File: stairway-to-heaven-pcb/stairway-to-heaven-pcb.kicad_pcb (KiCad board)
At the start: 2 copper layers, 15 parts, among them J1 Conn_01x04_Male, J2 Conn_01x04_Male, Q1 FDN337N, Q2 FDN337N, Q3 FDN337N, Q4 FDN337N, Q5 FDN337N, Q6 FDN337N, U1 MEGA_PRO_EMBED_CH340G_{slash}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

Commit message: update bom
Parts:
- moved R1 22.9 mm to (189.2, 116.8)
- moved R4 22.5 mm to (189.2, 100.3)
- moved Q1 21.6 mm to (194.3, 116.8), turned to 0 degrees
- moved Q4 21.6 mm to (194.3, 100.3), turned to 0 degrees
- moved R6 16.8 mm to (212.1, 95.2), turned to -90 degrees
- moved R3 16.7 mm to (212.1, 113.0), turned to -90 degrees
- moved Q6 11.5 mm to (217.2, 95.2), turned to 0 degrees
- moved Q3 11.4 mm to (217.2, 113.0), turned to 0 degrees
- moved R5 8.52 mm to (200.7, 97.8), turned to -90 degrees
- moved R2 8.13 mm to (200.7, 115.6)
- moved Q5 5.24 mm to (205.7, 97.8), turned to 0 degrees
- moved Q2 5.08 mm to (205.7, 115.6), turned to 0 degrees
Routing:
- net LED1B_GND: track 0.00 -> 35.7 mm
- net LED2B_GND: track 0.00 -> 33.3 mm
- net LED1B_EN: track 52.8 -> 29.7 mm
- net LED1R_GND: track 0.00 -> 22.3 mm
- net LED2R_GND: track 0.00 -> 21.9 mm
- net LED2B_EN: track 49.5 -> 29.1 mm
- net LED2G_EN: track 40.4 -> 54.7 mm
- net LED1G_EN: track 40.8 -> 53.5 mm
- net LED1G_GND: track 0.00 -> 11.8 mm
- net LED2G_GND: track 0.00 -> 10.4 mm
- net +12V: track 0.00 -> 8.62 mm
- net LED1R_EN: track 43.2 -> 37.3 mm
- net LED2R_EN: track 42.0 -> 39.1 mm

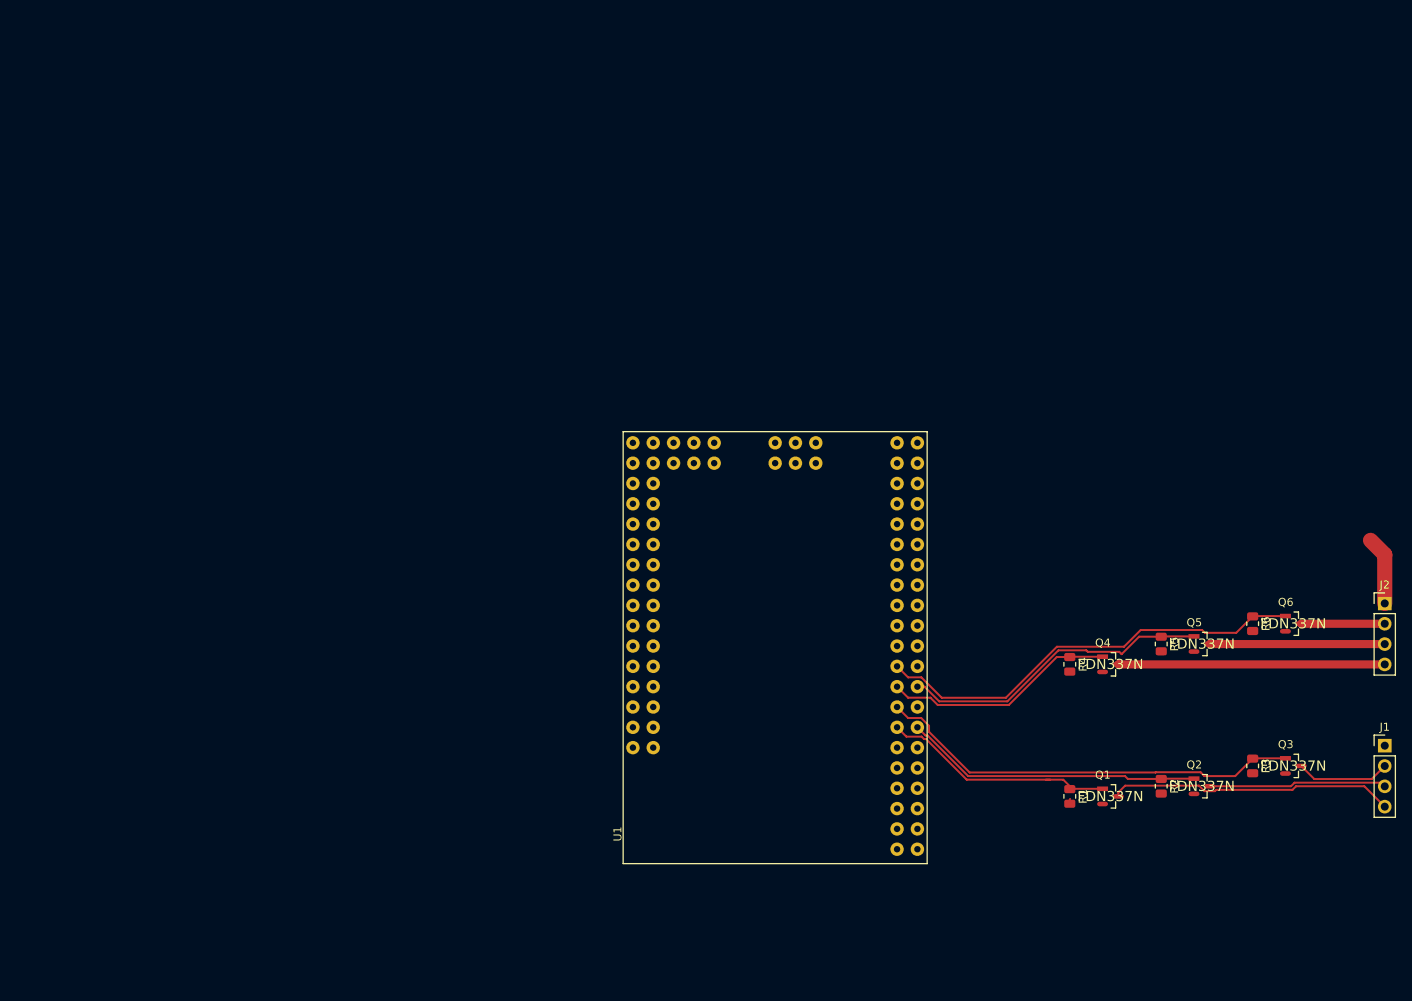
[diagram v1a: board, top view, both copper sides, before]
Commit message: Psu, hierachical pages for fet driver
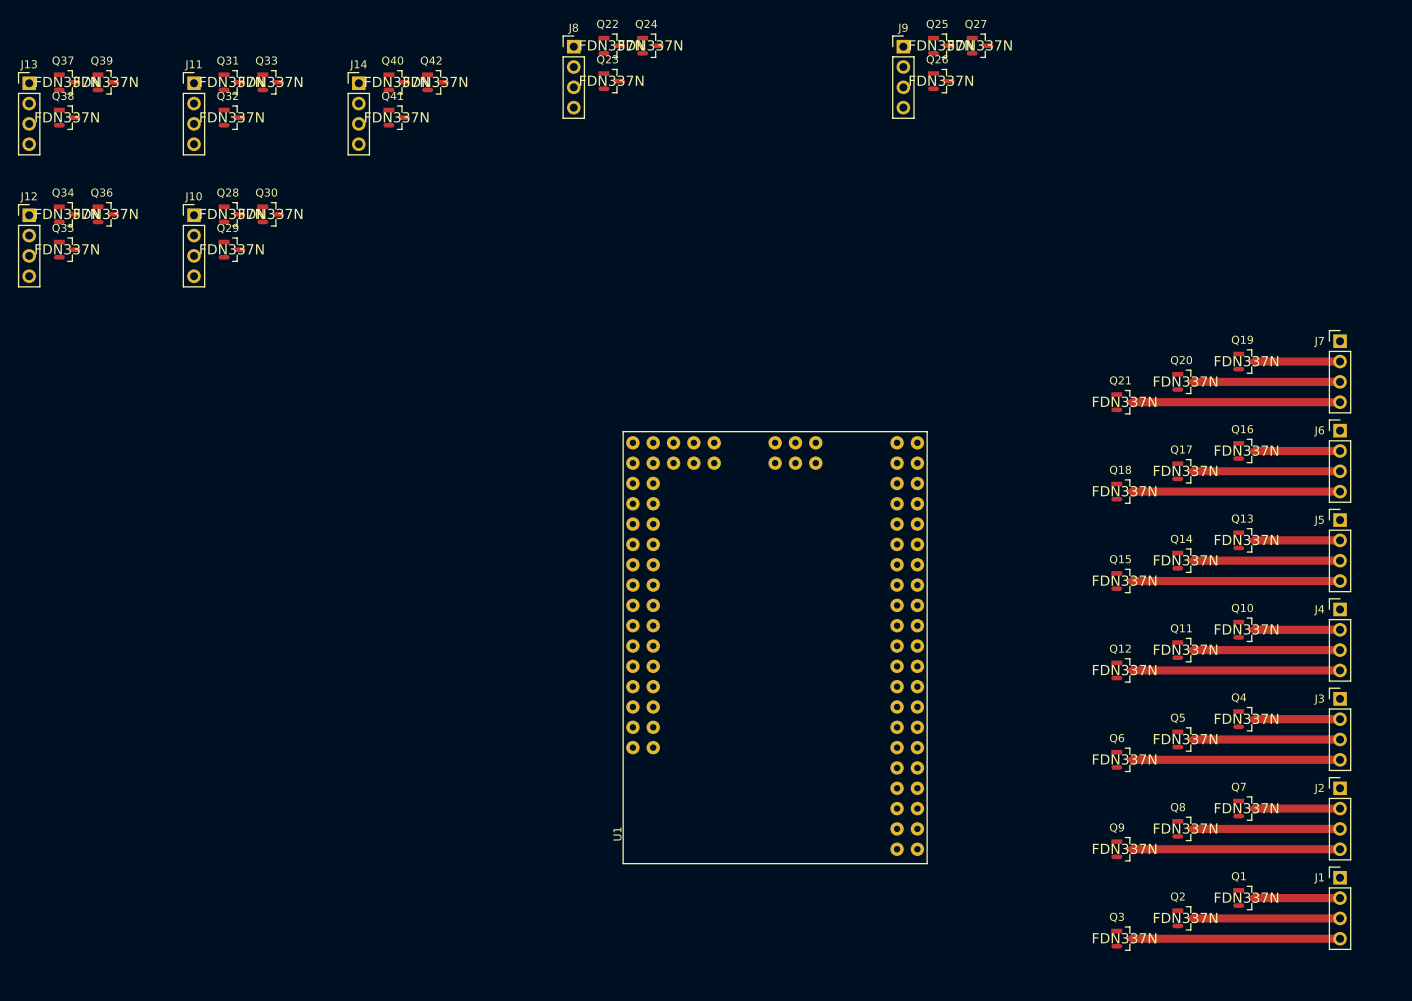
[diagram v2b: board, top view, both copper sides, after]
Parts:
- removed R1, R2, R3, R4, R5, R6: 50k, Resistor_SMD:R_0805_2012Metric
- added J10: Conn_01x04_Male, Connector_PinHeader_2.54mm:PinHeader_1x04_P2.54mm_Vertical, F.Cu at (79.8, 44.2)
- added J11: Conn_01x04_Male, Connector_PinHeader_2.54mm:PinHeader_1x04_P2.54mm_Vertical, F.Cu at (79.8, 27.7)
- added J12: Conn_01x04_Male, Connector_PinHeader_2.54mm:PinHeader_1x04_P2.54mm_Vertical, F.Cu at (59.2, 44.2)
- added J13: Conn_01x04_Male, Connector_PinHeader_2.54mm:PinHeader_1x04_P2.54mm_Vertical, F.Cu at (59.2, 27.7)
- added J14: Conn_01x04_Male, Connector_PinHeader_2.54mm:PinHeader_1x04_P2.54mm_Vertical, F.Cu at (100.4, 27.7)
- added J3: Conn_01x04_Male, Connector_PinHeader_2.54mm:PinHeader_1x04_P2.54mm_Vertical, F.Cu at (223.0, 104.6)
- added J4: Conn_01x04_Male, Connector_PinHeader_2.54mm:PinHeader_1x04_P2.54mm_Vertical, F.Cu at (223.0, 93.5)
- added J5: Conn_01x04_Male, Connector_PinHeader_2.54mm:PinHeader_1x04_P2.54mm_Vertical, F.Cu at (223.0, 82.3)
- added J6: Conn_01x04_Male, Connector_PinHeader_2.54mm:PinHeader_1x04_P2.54mm_Vertical, F.Cu at (223.0, 71.1)
- added J7: Conn_01x04_Male, Connector_PinHeader_2.54mm:PinHeader_1x04_P2.54mm_Vertical, F.Cu at (223.0, 59.9)
- added J8: Conn_01x04_Male, Connector_PinHeader_2.54mm:PinHeader_1x04_P2.54mm_Vertical, F.Cu at (127.2, 23.1)
- added J9: Conn_01x04_Male, Connector_PinHeader_2.54mm:PinHeader_1x04_P2.54mm_Vertical, F.Cu at (168.4, 23.1)
- added Q10: FDN337N, FDN337N:ON_Semi-527AG-01-12_2008-O-IPC_B, F.Cu at (211.3, 96.0)
- added Q11: FDN337N, FDN337N:ON_Semi-527AG-01-12_2008-O-IPC_B, F.Cu at (203.7, 98.6)
- added Q12: FDN337N, FDN337N:ON_Semi-527AG-01-12_2008-O-IPC_B, F.Cu at (196.1, 101.1)
- added Q13: FDN337N, FDN337N:ON_Semi-527AG-01-12_2008-O-IPC_B, F.Cu at (211.3, 84.8)
- added Q14: FDN337N, FDN337N:ON_Semi-527AG-01-12_2008-O-IPC_B, F.Cu at (203.7, 87.4)
- added Q15: FDN337N, FDN337N:ON_Semi-527AG-01-12_2008-O-IPC_B, F.Cu at (196.1, 89.9)
- added Q16: FDN337N, FDN337N:ON_Semi-527AG-01-12_2008-O-IPC_B, F.Cu at (211.3, 73.7)
- added Q17: FDN337N, FDN337N:ON_Semi-527AG-01-12_2008-O-IPC_B, F.Cu at (203.7, 76.2)
- added Q18: FDN337N, FDN337N:ON_Semi-527AG-01-12_2008-O-IPC_B, F.Cu at (196.1, 78.7)
- added Q19: FDN337N, FDN337N:ON_Semi-527AG-01-12_2008-O-IPC_B, F.Cu at (211.3, 62.5)
- added Q20: FDN337N, FDN337N:ON_Semi-527AG-01-12_2008-O-IPC_B, F.Cu at (203.7, 65.0)
- added Q21: FDN337N, FDN337N:ON_Semi-527AG-01-12_2008-O-IPC_B, F.Cu at (196.1, 67.6)
- added Q22: FDN337N, FDN337N:ON_Semi-527AG-01-12_2008-O-IPC_B, F.Cu at (132.0, 23.0)
- added Q23: FDN337N, FDN337N:ON_Semi-527AG-01-12_2008-O-IPC_B, F.Cu at (132.0, 27.4)
- added Q24: FDN337N, FDN337N:ON_Semi-527AG-01-12_2008-O-IPC_B, F.Cu at (136.8, 23.0)
- added Q25: FDN337N, FDN337N:ON_Semi-527AG-01-12_2008-O-IPC_B, F.Cu at (173.2, 23.0)
- added Q26: FDN337N, FDN337N:ON_Semi-527AG-01-12_2008-O-IPC_B, F.Cu at (173.2, 27.4)
- added Q27: FDN337N, FDN337N:ON_Semi-527AG-01-12_2008-O-IPC_B, F.Cu at (178.0, 23.0)
- added Q28: FDN337N, FDN337N:ON_Semi-527AG-01-12_2008-O-IPC_B, F.Cu at (84.5, 44.1)
- added Q29: FDN337N, FDN337N:ON_Semi-527AG-01-12_2008-O-IPC_B, F.Cu at (84.5, 48.5)
- added Q30: FDN337N, FDN337N:ON_Semi-527AG-01-12_2008-O-IPC_B, F.Cu at (89.3, 44.1)
- added Q31: FDN337N, FDN337N:ON_Semi-527AG-01-12_2008-O-IPC_B, F.Cu at (84.5, 27.6)
- added Q32: FDN337N, FDN337N:ON_Semi-527AG-01-12_2008-O-IPC_B, F.Cu at (84.5, 32.0)
- added Q33: FDN337N, FDN337N:ON_Semi-527AG-01-12_2008-O-IPC_B, F.Cu at (89.3, 27.6)
- added Q34: FDN337N, FDN337N:ON_Semi-527AG-01-12_2008-O-IPC_B, F.Cu at (63.9, 44.1)
- added Q35: FDN337N, FDN337N:ON_Semi-527AG-01-12_2008-O-IPC_B, F.Cu at (63.9, 48.5)
- added Q36: FDN337N, FDN337N:ON_Semi-527AG-01-12_2008-O-IPC_B, F.Cu at (68.7, 44.1)
- added Q37: FDN337N, FDN337N:ON_Semi-527AG-01-12_2008-O-IPC_B, F.Cu at (63.9, 27.6)
- added Q38: FDN337N, FDN337N:ON_Semi-527AG-01-12_2008-O-IPC_B, F.Cu at (63.9, 32.0)
- added Q39: FDN337N, FDN337N:ON_Semi-527AG-01-12_2008-O-IPC_B, F.Cu at (68.7, 27.6)
- added Q40: FDN337N, FDN337N:ON_Semi-527AG-01-12_2008-O-IPC_B, F.Cu at (105.1, 27.6)
- added Q41: FDN337N, FDN337N:ON_Semi-527AG-01-12_2008-O-IPC_B, F.Cu at (105.1, 32.0)
- added Q42: FDN337N, FDN337N:ON_Semi-527AG-01-12_2008-O-IPC_B, F.Cu at (109.9, 27.6)
- added Q7: FDN337N, FDN337N:ON_Semi-527AG-01-12_2008-O-IPC_B, F.Cu at (211.3, 118.4)
- added Q8: FDN337N, FDN337N:ON_Semi-527AG-01-12_2008-O-IPC_B, F.Cu at (203.7, 120.9)
- added Q9: FDN337N, FDN337N:ON_Semi-527AG-01-12_2008-O-IPC_B, F.Cu at (196.1, 123.4)
- moved Q3 30.2 mm to (196.1, 134.6)
- moved Q6 27.1 mm to (196.1, 112.3)
- moved J2 23.8 mm to (223.0, 115.8)
- moved Q1 21.2 mm to (211.3, 129.5)
- moved Q4 18.3 mm to (211.3, 107.2)
- moved J1 17.4 mm to (223.0, 127.0)
- moved Q2 16.6 mm to (203.7, 132.1)
- moved Q5 12.1 mm to (203.7, 109.7)
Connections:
- net LED1R_EN renamed /LED1R_EN
- net LED1R_GND renamed Net-(J1-Pad3)
- J1 pad 2: LED1G_GND -> Net-(J1-Pad2)
- J1 pad 4: LED1B_GND -> Net-(J1-Pad4)
- J2 pad 2: LED2G_GND -> Net-(J3-Pad2)
- J2 pad 3: LED2R_GND -> Net-(J3-Pad3)
- J2 pad 4: LED2B_GND -> Net-(J3-Pad4)
- Q1 pad 1: LED1B_EN -> /Fets1/G_EN
- Q1 pad 2: LED1B_GND -> Net-(J1-Pad2)
- Q3 pad 1: LED1G_EN -> /Fets1/B_EN
- Q3 pad 2: LED1G_GND -> Net-(J1-Pad4)
- Q4 pad 1: LED2B_EN -> /Fets3/G_EN
- Q4 pad 2: LED2B_GND -> Net-(J2-Pad2)
- Q5 pad 1: LED2R_EN -> /LED3R_EN
- Q5 pad 2: LED2R_GND -> Net-(J2-Pad3)
- Q6 pad 1: LED2G_EN -> /Fets3/B_EN
- Q6 pad 2: LED2G_GND -> Net-(J2-Pad4)
- U1 pad D10: LED3R_EN -> /LED3R_EN
- U1 pad D11: LED3G_EN -> /Fets3/G_EN
- U1 pad D13: LED4B_EN -> /Fets4/B_EN
- U1 pad D14: LED4R_EN -> /LED4R_EN
- U1 pad D15: LED4G_EN -> /Fets4/G_EN
- U1 pad D16: LED5B_EN -> /Fets5/B_EN
- U1 pad D17: LED5R_EN -> /LED5R_EN
- U1 pad D18: LED5G_EN -> /Fets5/G_EN
- U1 pad D2: LED1B_EN -> /Fets1/B_EN
- U1 pad D20: LED6B_EN -> /Fets6/B_EN
- U1 pad D21: LED6R_EN -> /LED6R_EN
- U1 pad D22: LED6G_EN -> /Fets6/G_EN
- U1 pad D23: LED7B_EN -> /Fets7/B_EN
- U1 pad D24: LED7R_EN -> /LED7R_EN
- U1 pad D25: LED7G_EN -> /Fets7/G_EN
- U1 pad D27: LED8B_EN -> /Fets8/B_EN
- U1 pad D28: LED8R_EN -> /LED8R_EN
- U1 pad D29: LED8G_EN -> /Fets8/G_EN
- U1 pad D30: LED9B_EN -> /Fets9/B_EN
- U1 pad D31: LED9R_EN -> /LED9R_EN
- U1 pad D32: LED9G_EN -> /Fets9/G_EN
- U1 pad D34: unconnected-(U1-PadD34) -> /Fets10/B_EN
- U1 pad D35: unconnected-(U1-PadD35) -> /LED10R_EN
- U1 pad D36: unconnected-(U1-PadD36) -> /Fets10/G_EN
- U1 pad D37: unconnected-(U1-PadD37) -> /Fets11/B_EN
- U1 pad D38: unconnected-(U1-PadD38) -> /LED11R_EN
- U1 pad D39: unconnected-(U1-PadD39) -> /Fets11/G_EN
- U1 pad D4: LED1G_EN -> /Fets1/G_EN
- U1 pad D41: unconnected-(U1-PadD41) -> /Fets12/B_EN
- U1 pad D42: unconnected-(U1-PadD42) -> /LED12R_EN
- U1 pad D43: unconnected-(U1-PadD43) -> /Fets12/G_EN
- U1 pad D44: unconnected-(U1-PadD44) -> /Fets13/B_EN
- U1 pad D45: unconnected-(U1-PadD45) -> /LED13R_EN
- U1 pad D46: unconnected-(U1-PadD46) -> /Fets13/G_EN
- U1 pad D48: unconnected-(U1-PadD48) -> /Fets14/B_EN
- U1 pad D49: unconnected-(U1-PadD49) -> /LED14R_EN
- U1 pad D50: unconnected-(U1-PadD50) -> /Fets14/G_EN
- U1 pad D6: LED2B_EN -> /Fets2/B_EN
- U1 pad D7: LED2R_EN -> /LED2R_EN
- U1 pad D8: LED2G_EN -> /Fets2/G_EN
- U1 pad D9: LED3B_EN -> /Fets3/B_EN
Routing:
- net LED2G_EN: track 54.7 -> 0.00 mm
- net LED1G_EN: track 53.5 -> 0.00 mm
- net LED2R_EN: track 39.1 -> 0.00 mm
- net /LED1R_EN: track 37.3 -> 0.00 mm
- net LED1B_GND: track 35.7 -> 0.00 mm
- net LED2B_GND: track 33.3 -> 0.00 mm
- net LED1B_EN: track 29.7 -> 0.00 mm
- net LED2B_EN: track 29.1 -> 0.00 mm
- net Net-(J1-Pad4): track 0.00 -> 25.9 mm
- net Net-(J7-Pad4): track 0.00 -> 25.9 mm
- net Net-(J6-Pad4): track 0.00 -> 25.9 mm
- net Net-(J5-Pad4): track 0.00 -> 25.9 mm
- net Net-(J4-Pad4): track 0.00 -> 25.9 mm
- net Net-(J3-Pad4): track 0.00 -> 25.9 mm
- net Net-(J2-Pad4): track 0.00 -> 25.9 mm
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
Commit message: initial pcb placement and routing tests
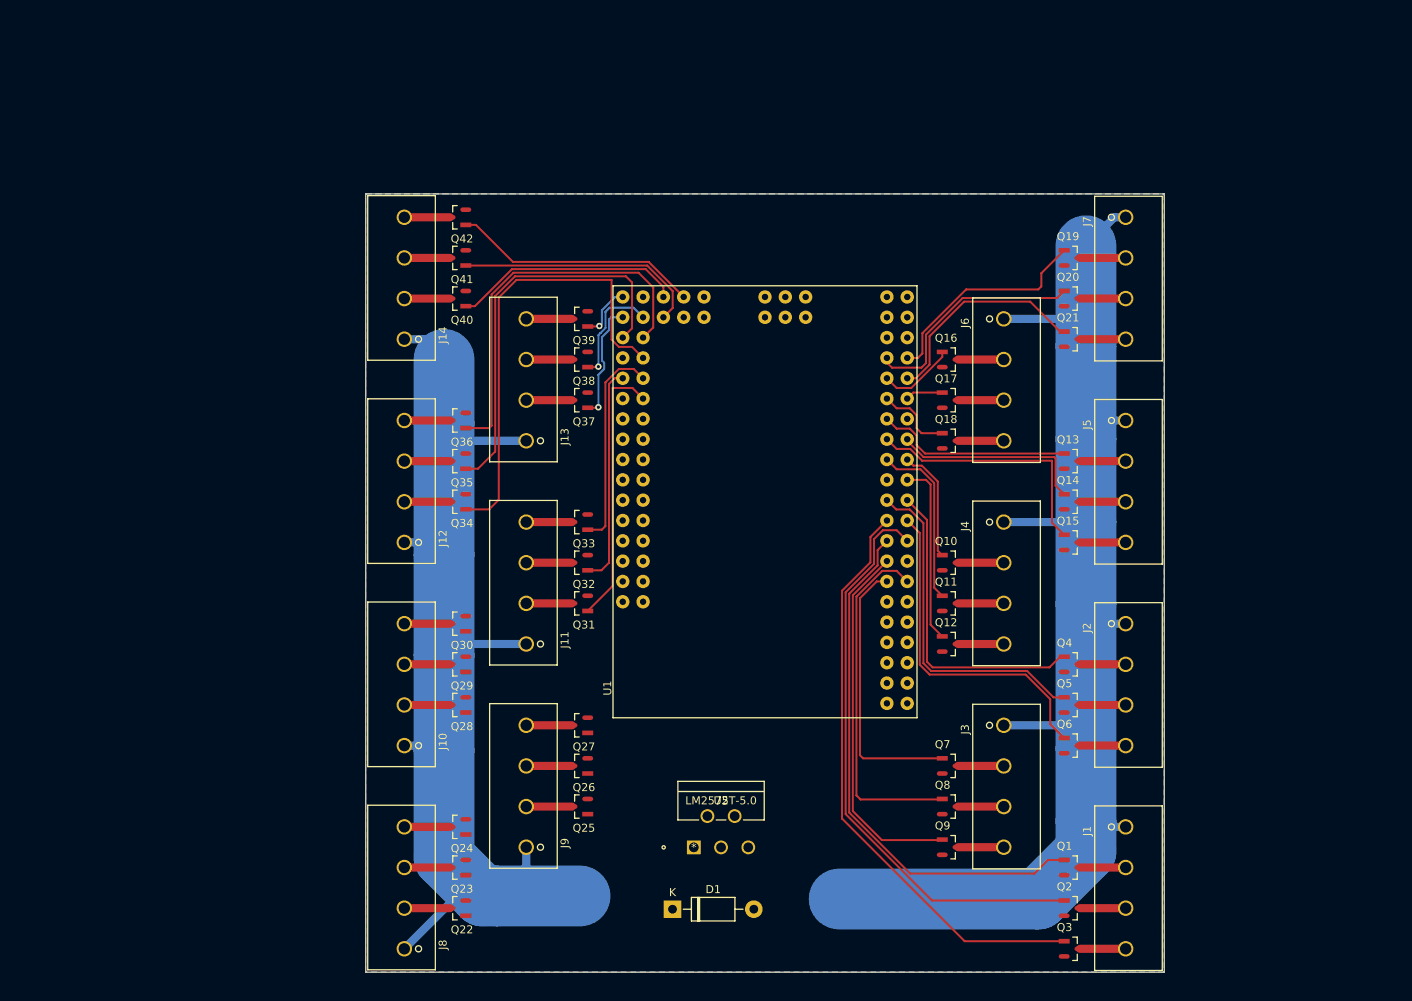
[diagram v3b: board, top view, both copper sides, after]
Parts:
- added D1: 1N5819, Diode_THT:D_DO-41_SOD81_P10.16mm_Horizontal, F.Cu at (139.6, 130.9)
- added U2: LM2575T-5.0, kicad-ss-libs:LM2576T-ADJG, F.Cu at (142.2, 123.2)
- J1, J10, J11, J12, J13, J14, J4, J5, J6, J7, J8, J9: footprint Connector_PinHeader_2.54mm:PinHeader_1x04_P2.54mm_Vertical -> kicad-ss-libs:ScrewTerminal-5_08
- J2: renamed from J3; footprint Connector_PinHeader_2.54mm:PinHeader_1x04_P2.54mm_Vertical -> kicad-ss-libs:ScrewTerminal-5_08
- J3: renamed from J2; footprint Connector_PinHeader_2.54mm:PinHeader_1x04_P2.54mm_Vertical -> kicad-ss-libs:ScrewTerminal-5_08
- moved J8 114.7 mm to (106.0, 135.9), turned to 90 degrees
- moved J9 110.6 mm to (121.3, 123.2), turned to 90 degrees
- moved Q22 109.5 mm to (112.7, 130.8), turned to 180 degrees
- moved Q25 105.3 mm to (128.0, 118.1), turned to 180 degrees
- moved Q24 100.6 mm to (112.7, 120.7), turned to 180 degrees
- moved Q23 100.2 mm to (112.7, 125.7), turned to 180 degrees
- moved Q27 98.6 mm to (128.0, 108.0), turned to 180 degrees
- moved Q26 96.8 mm to (128.0, 113.0), turned to 180 degrees
- moved J11 81.5 mm to (121.3, 97.8), turned to 90 degrees
- moved Q31 78.3 mm to (128.0, 92.7), turned to 180 degrees
- moved J13 76.5 mm to (121.3, 72.4), turned to 90 degrees
- moved Q37 75.4 mm to (128.0, 67.3), turned to 180 degrees
- moved J10 71.3 mm to (106.0, 110.5), turned to 90 degrees
- moved Q38 70.9 mm to (128.0, 62.2), turned to 180 degrees
- moved Q32 70.6 mm to (128.0, 87.6), turned to 180 degrees
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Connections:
- U1 pad 5V_1: unconnected-(U1-Pad5V_1) -> +5V
- U1 pad 5V_2: unconnected-(U1-Pad5V_1) -> +5V
- U1 pad 5V_3: unconnected-(U1-Pad5V_1) -> +5V
- U1 pad D2: /Fets1/B_EN -> /Fets2/G_EN
- U1 pad D3: /LED1R_EN -> /LED2R_EN
- U1 pad D37: /Fets11/B_EN -> /Fets11/G_EN
- U1 pad D39: /Fets11/G_EN -> /Fets11/B_EN
- U1 pad D4: /Fets1/G_EN -> /Fets2/B_EN
- U1 pad D41: /Fets12/B_EN -> /Fets12/G_EN
- U1 pad D43: /Fets12/G_EN -> /Fets12/B_EN
- U1 pad D44: /Fets13/B_EN -> /Fets13/G_EN
- U1 pad D46: /Fets13/G_EN -> /Fets13/B_EN
- U1 pad D48: /Fets14/B_EN -> /Fets14/G_EN
- U1 pad D50: /Fets14/G_EN -> /Fets14/B_EN
- U1 pad D6: /Fets2/B_EN -> /Fets1/G_EN
- U1 pad D7: /LED2R_EN -> /LED1R_EN
- U1 pad D8: /Fets2/G_EN -> /Fets1/B_EN
- U1 pad VIN_1: +12V -> unconnected-(U1-PadVIN_1)
- U1 pad VIN_2: +12V -> unconnected-(U1-PadVIN_1)
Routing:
- net +12V: track 0.00 -> 306.3 mm
- net /Fets1/B_EN: track 0.00 -> 73.7 mm
- net /LED1R_EN: track 0.00 -> 72.8 mm
- net /Fets1/G_EN: track 0.00 -> 66.7 mm
- net /Fets12/G_EN: track 0.00 -> 57.3 mm
- net /LED12R_EN: track 0.00 -> 49.8 mm
- net /Fets12/B_EN: track 0.00 -> 48.6 mm
- net /Fets2/B_EN: track 0.00 -> 45.7 mm
- net /LED2R_EN: track 0.00 -> 44.0 mm
- net /LED3R_EN: track 0.00 -> 42.6 mm
- net /Fets3/B_EN: track 0.00 -> 42.3 mm
- net /Fets3/G_EN: track 0.00 -> 39.2 mm
- net /Fets2/G_EN: track 0.00 -> 34.3 mm
- net /Fets11/G_EN: track 0.00 -> 33.5 mm
- net /Fets5/B_EN: track 0.00 -> 31.6 mm
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- added copper zone on B.Cu, net GND
- added copper zone on F.Cu, net GND
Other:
- board outline added: 99.8 x 97.3 mm

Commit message: psu layout
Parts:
- added C1: 47uF, Capacitor_SMD:C_Elec_6.3x5.8, F.Cu at (162.4, 121.0)
- added C2: 100uF, Capacitor_SMD:C_Elec_8x6.2, B.Cu at (143.7, 101.3)
- added C3: 10uF, Capacitor_SMD:C_1206_3216Metric, F.Cu at (155.9, 122.4)
- added C4: 100uF, Capacitor_SMD:C_Elec_8x6.2, B.Cu at (155.9, 103.8)
- added C5: 10uF, Capacitor_SMD:C_1206_3216Metric, B.Cu at (148.0, 111.1)
- added C6: 10uF, Capacitor_SMD:C_1206_3216Metric, B.Cu at (149.5, 107.4)
- added J15: PJ-063AH, kicad-ss-libs:CUI_PJ-063AH, F.Cu at (159.1, 128.4)
- added L1: 100uH, Inductor_SMD:L_10.4x10.4_H4.8, B.Cu at (143.6, 113.4)
- D1: value 1N5819 -> DO-214AC; footprint Diode_THT:D_DO-41_SOD81_P10.16mm_Horizontal -> Diode_SMD:D_SMA; moved to B.Cu
- U2: footprint kicad-ss-libs:LM2576T-ADJG -> kicad-ss-libs:LM2575T-5.0
- moved D1 10.3 mm to (143.8, 121.6), turned to 180 degrees
- moved U2 10.2 mm to (150.8, 117.5), turned to 180 degrees
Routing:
- net +5V: track 0.00 -> 102.0 mm
- net +12V: track 306.3 -> 356.4 mm
- net Net-(D1-Pad1): track 0.00 -> 9.98 mm
- net /Fets2/G_EN: track 34.3 -> 25.4 mm
- net /LED2R_EN: track 44.0 -> 37.2 mm
- net /Fets1/G_EN: track 66.7 -> 62.9 mm
- net /Fets2/B_EN: track 45.7 -> 41.9 mm
- net /Fets1/B_EN: track 73.7 -> 74.8 mm
- net GND: vias 0 -> 82
